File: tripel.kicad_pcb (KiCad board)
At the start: 2 copper layers, 95.1 x 97.5 mm, 64 parts, among them J1 Left Columns, J2 Left Rows, J3 Right Rows, J4 Right Columns, J5 Left Rows, J6 USB_mini_micro_B, J7 Conn_01x04, J8 Right Rows, K1.1 KEYSW, K1.2 KEYSW, K1.3 KEYSW, K1.4 KEYSW, K1.5 KEYSW, K2.1 KEYSW, K2.2 KEYSW, K2.3 KEYSW, K2.4 KEYSW, K2.5 KEYSW, K3.1 KEYSW, K3.2 KEYSW, K3.3 KEYSW, K3.4 KEYSW, K3.5 KEYSW, K4.1 KEYSW, K4.2 KEYSW, K4.3 KEYSW, K4.4 KEYSW, K4.5 KEYSW, K5.1 KEYSW, K5.2 KEYSW, K5.3 KEYSW, K5.4 KEYSW, K5.5 KEYSW, K5.6 KEYSW, K5.7 KEYSW, K5.8 KEYSW, U1 ProMicro_ChipSideDown

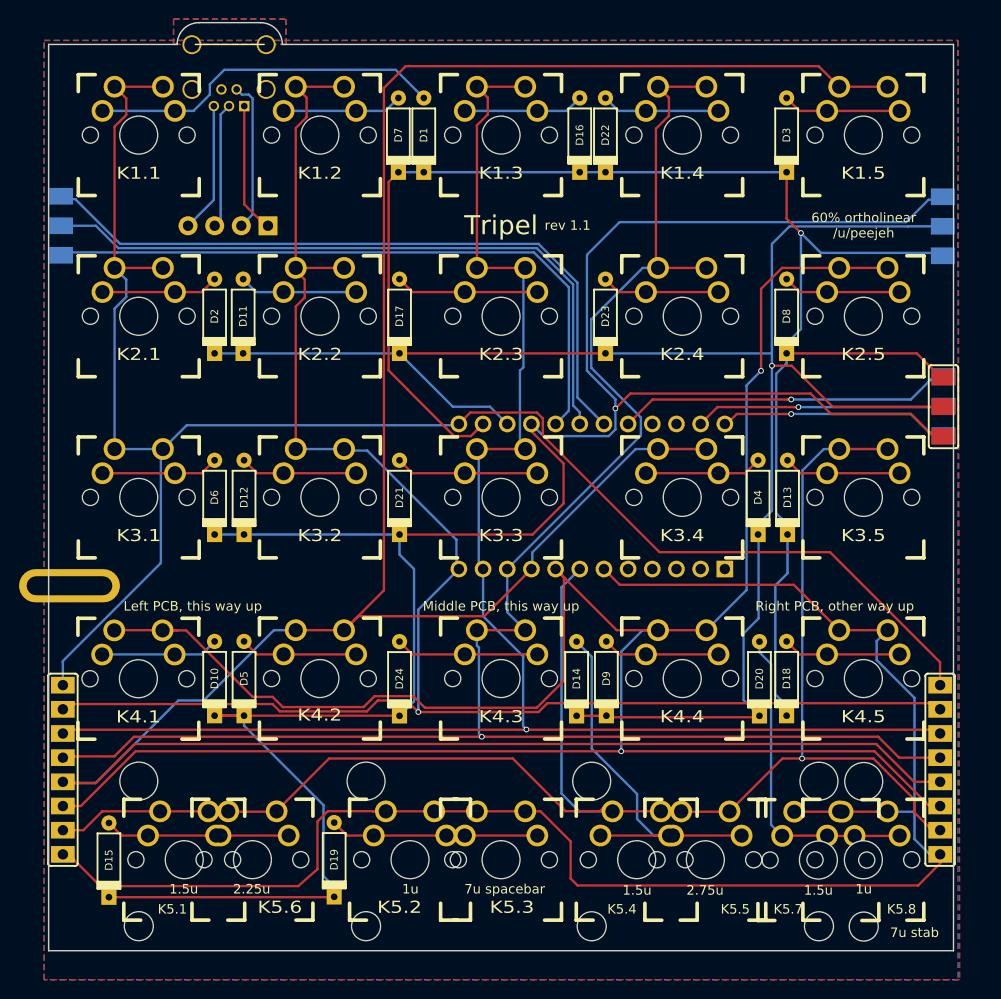
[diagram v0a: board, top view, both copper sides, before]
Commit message: Switch to single sided design
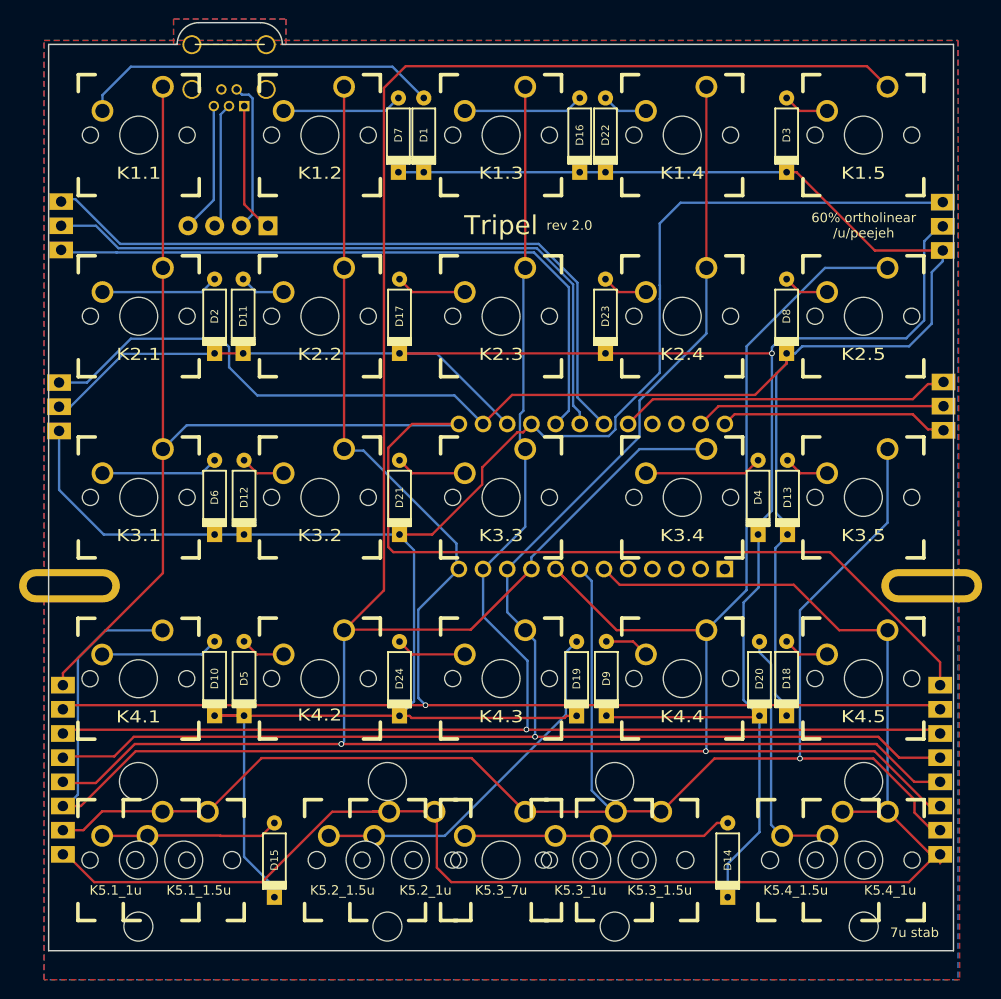
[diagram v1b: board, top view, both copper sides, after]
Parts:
- removed K5.3, K5.8: KEYSW, keyboard:MX_DOUBLESIDED
- removed K5.4: KEYSW, keyboard:MX_DBL_150
- removed K5.5: KEYSW, keyboard:MX_DBL_275
- removed K5.6: KEYSW, keyboard:MX_DBL_225
- added K5.1_1u: KEYSW, keyboard:MX, F.Cu at (121.3, 123.8)
- added K5.2_1.5u: KEYSW, keyboard:MX_PCB_150H, F.Cu at (145.1, 123.8)
- added K5.3_1.5u: KEYSW, keyboard:MX_PCB_150H, F.Cu at (173.7, 123.8)
- added K5.3_1u: KEYSW, keyboard:MX, F.Cu at (168.9, 123.8)
- added K5.3_7u: KEYSW, keyboard:MX_PCB_200H, F.Cu at (159.4, 123.8)
- added K5.4_1u: KEYSW, keyboard:MX, F.Cu at (197.5, 123.8)
- added REF**: Mounting M2, footprints:Mounting_M2, F.Cu at (204.6, 95.0)
- added REF**: MountingHole_3mm, MountingHole:MountingHole_3mm, F.Cu at (121.3, 130.8)
- added REF**: MountingHole_3mm, MountingHole:MountingHole_3mm, F.Cu at (121.3, 115.5)
- J1, J4, J8: moved to B.Cu
- K1.1, K1.2, K1.3, K1.4, K1.5, K2.1, K2.2, K2.3, K2.4, K2.5, K3.1, K3.2, K3.3, K3.4, K3.5, K4.1, K4.2, K4.3, K4.4, K4.5: footprint keyboard:MX_DOUBLESIDED -> keyboard:MX
- K5.1_1.5u: renamed from K5.1; footprint keyboard:MX_DBL_150 -> keyboard:MX_PCB_150H
- K5.2_1u: renamed from K5.2; footprint keyboard:MX_DOUBLESIDED -> keyboard:MX
- K5.4_1.5u: renamed from K5.7; footprint keyboard:MX_DBL_150 -> keyboard:MX_PCB_150H
- moved J8 92.9 mm to (112.9, 76.2)
- moved D19 31.8 mm to (167.3, 104.7)
- moved D14 24.8 mm to (183.2, 123.8)
- moved D15 17.4 mm to (135.6, 123.8)
- moved K5.1_1.5u 0.07 mm to (126.0, 123.8)
- moved K5.2_1u 0.05 mm to (149.8, 123.8)
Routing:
- net Net-(J1-Pad3): track 251.6 -> 206.5 mm, vias 2 -> 1
- net Net-(D1-Pad1): track 169.1 -> 212.3 mm, vias 1 -> 0
- net Net-(D10-Pad1): track 244.0 -> 210.1 mm, vias 1 -> 0
- net Net-(J1-Pad4): track 292.2 -> 268.1 mm, vias 0 -> 1
- net Net-(J1-Pad7): track 185.6 -> 166.3 mm
- net Net-(J1-Pad5): track 191.5 -> 172.1 mm
- net Net-(D19-Pad2): track 21.9 -> 38.3 mm
- net Net-(J1-Pad6): track 179.7 -> 164.9 mm
- net Net-(D11-Pad1): track 182.4 -> 197.1 mm
- net Net-(D14-Pad2): track 40.2 -> 28.2 mm
- net Net-(J1-Pad1): track 181.8 -> 172.4 mm
- net Net-(D8-Pad2): track 12.4 -> 4.82 mm
- net Net-(D24-Pad2): track 15.0 -> 7.41 mm
- net Net-(D23-Pad2): track 12.4 -> 4.82 mm
- net Net-(D20-Pad2): track 33.8 -> 26.1 mm
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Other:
- board text added: "To left PCB"
- board text added: "To right PCB"
- board text added: "rev 2.0"
- board text removed: "1.5u"
- board text removed: "1u"
- board text removed: "2.25u"
- board text removed: "2.75u"
- board text removed: "7u spacebar"
- board text removed: "Left PCB, this way up"
- board text removed: "Middle PCB, this way up"
- board text removed: "Right PCB, other way up"
- board text removed: "rev 1.1"

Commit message: Add some backside silkscreen patterns
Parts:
- added REF**: Tripel, keyboard:Tripel, B.Cu at (151.4, 126.2)
- added REF**: Tripel, keyboard:Tripel, B.Cu at (98.3, 54.3)
- added REF**: Tripel, keyboard:Tripel, B.Cu at (193.5, 54.3)
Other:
- board text added: "EL"
- board text added: "TRIP"
- board text added: "TRIPEL"

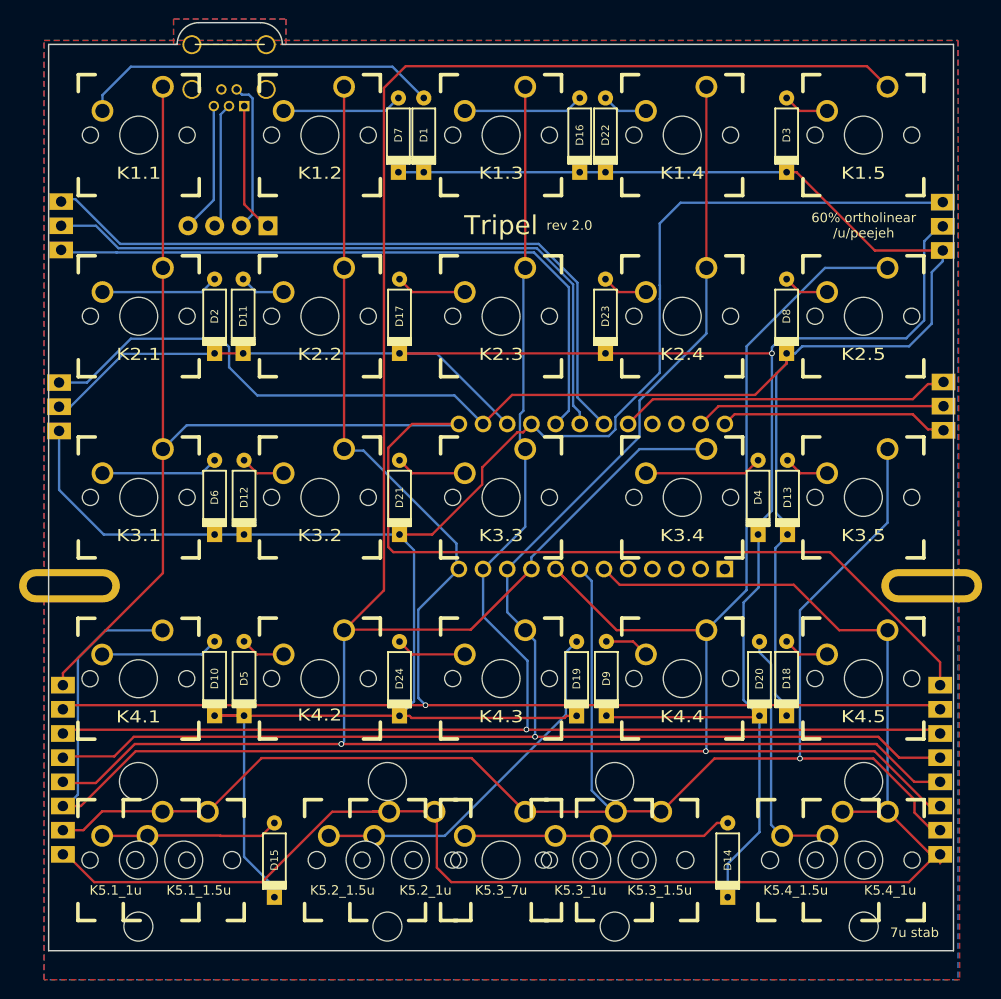
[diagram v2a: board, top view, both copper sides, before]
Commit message: Add 4x1u bottom row option
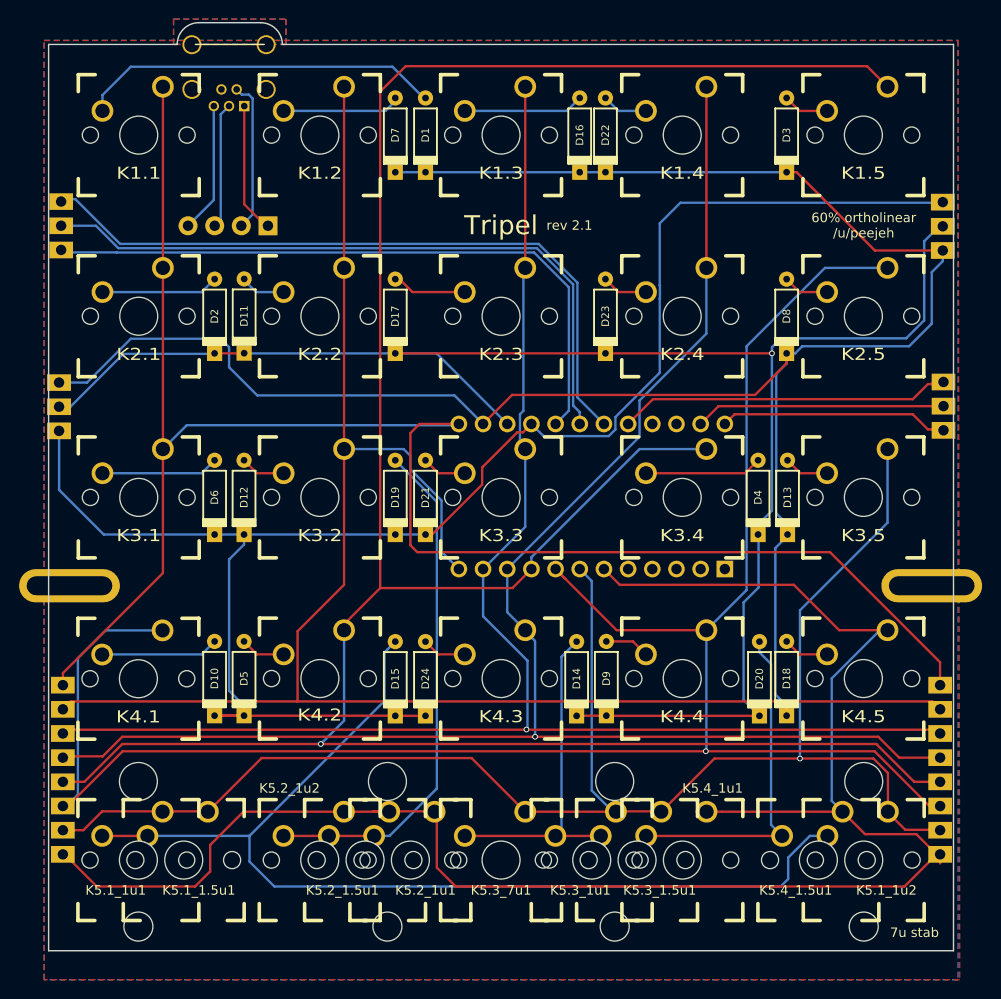
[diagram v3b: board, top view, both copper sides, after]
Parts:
- removed K5.1_1u, K5.4_1u: KEYSW, keyboard:MX
- removed K5.3_7u: KEYSW, keyboard:MX_PCB_200H
- added K5.1_1u1: KEYSW, keyboard:MX, F.Cu at (121.3, 123.8)
- added K5.1_1u2: KEYSW, keyboard:MX, F.Cu at (197.5, 123.8)
- added K5.2_1u2: KEYSW, keyboard:MX, F.Cu at (140.3, 123.8)
- added K5.3_7u1: KEYSW, keyboard:MX_PCB_200H, F.Cu at (159.4, 123.8)
- added K5.4_1u1: KEYSW, keyboard:MX, F.Cu at (178.4, 123.8)
- moved D19 26.9 mm to (148.3, 85.7)
- moved D14 24.8 mm to (167.3, 104.7)
- moved D15 22.9 mm to (148.3, 104.7)
- moved D21 2.73 mm to (151.4, 85.7)
- moved D24 2.73 mm to (151.4, 104.7)
- moved D17 0.44 mm to (148.3, 66.7)
- moved D7 0.33 mm to (148.3, 47.6)
- moved D1 0.18 mm to (151.4, 47.6)
- moved D11 0.11 mm to (132.4, 66.6)
- renumbered K5.1_1.5u to K5.1_1.5u1, K5.2_1.5u to K5.2_1.5u1, K5.2_1u to K5.2_1u1, K5.3_1.5u to K5.3_1.5u1, K5.3_1u to K5.3_1u1, K5.4_1.5u to K5.4_1.5u1
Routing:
- net Net-(D15-Pad2): track 18.7 -> 110.3 mm
- net Net-(D10-Pad1): track 210.1 -> 173.0 mm
- net Net-(J1-Pad1): track 172.4 -> 191.8 mm
- net Net-(D11-Pad1): track 197.1 -> 180.2 mm
- net Net-(D19-Pad2): track 38.3 -> 54.5 mm
- net Net-(J1-Pad7): track 166.3 -> 181.3 mm, vias 1 -> 0
- net Net-(D20-Pad2): track 26.1 -> 35.7 mm
- net Net-(D14-Pad2): track 28.2 -> 35.6 mm
- net Net-(J1-Pad4): track 268.1 -> 263.2 mm
- net Net-(J1-Pad8): track 183.7 -> 179.8 mm
- net Net-(D24-Pad2): track 7.41 -> 4.68 mm
- net Net-(D21-Pad2): track 7.42 -> 4.69 mm
- net Net-(J1-Pad2): track 167.8 -> 169.4 mm
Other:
- board text added: "rev 2.1"
- board text removed: "rev 2.0"
